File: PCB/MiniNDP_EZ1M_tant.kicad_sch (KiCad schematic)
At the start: 16 parts, among them J1 Conn_02x20_Odd_Even, U1 AS6C8008_TSOPII, U2 HC238, U3 4040, U4 FCT841

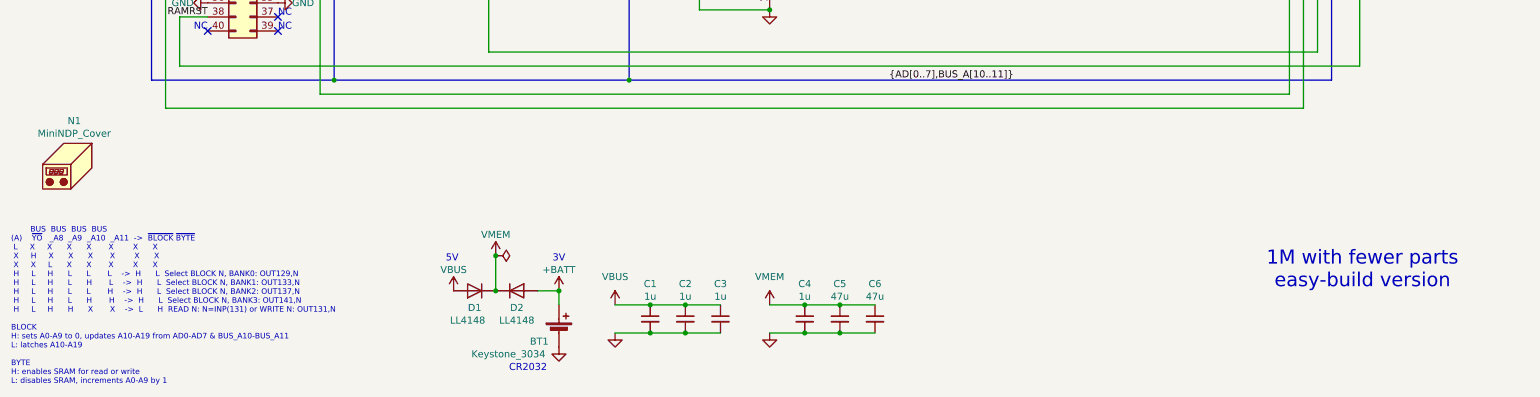
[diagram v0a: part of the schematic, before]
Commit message: make EZ1M the default
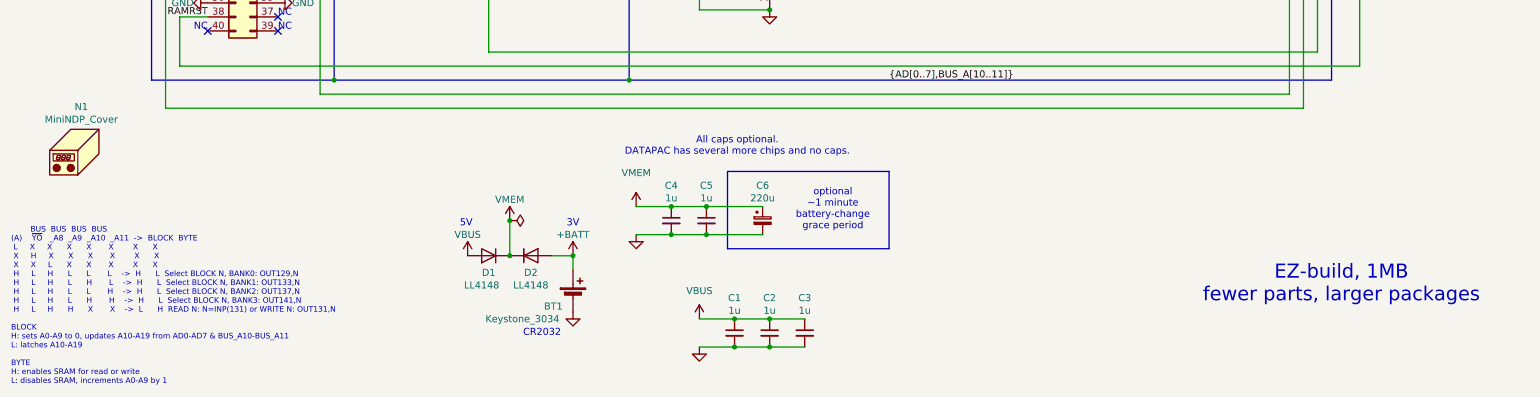
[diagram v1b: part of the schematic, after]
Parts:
- removed C6: 47u, 000_LOCAL:C_1206, symbol 000_LOCAL:C
- added C4: 1u, 000_LOCAL:C_0805, symbol 000_LOCAL:C
- C6: renamed from C5; value 47u -> 220u; footprint 000_LOCAL:C_1206 -> 000_LOCAL:CP_6032; symbol 000_LOCAL:C -> 000_LOCAL:C_Polarized; MPN C3216X5R1E476M160DC -> TAJC227K010RNJ
- renumbered C4 to C5
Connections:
- net GND: now also C4.2
- net VMEM: now also C4.1
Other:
- note added: "All caps optional. DATAPAC has several more chips and no caps."
- note added: "BUS BUS BUS BUS (A) ~{YO} _A8 _A9 _A10 _A11 -> BLOCK BYTE L X X X X X X X X H X X X X X X X X L X X X X X H L H L L L -> H L Select BLOCK N, BANK0: OUT129,N H L H L H L -> H L Select BLOCK N, BANK1: OUT133,N H L H L L H -> H L Select BLOCK N, BANK2: OUT137,N H L H L H H -> H L Select BLOCK N, BANK3: OUT141,N H L H H X X -> L H READ N: N=INP(131) or WRITE N: OUT131,N BLOCK H: sets A0-A9 to 0, upda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"
- note added: "EZ-build, 1MB fewer parts, larger packages"
- note added: "optional ~1 minute battery-change grace period"
- note removed: "1M with fewer parts easy-build version"
- note removed: "BUS BUS BUS BUS (A) ~{YO} _A8 _A9 _A10 _A11 -> ~{BLOCK} ~{BYTE} L X X X X X X X X H X X X X X X X X L X X X X X H L H L L L -> H L Select BLOCK N, BANK0: OUT129,N H L H L H L -> H L Select BLOCK N, BANK1: OUT133,N H L H L L H -> H L Select BLOCK N, BANK2: OUT137,N H L H L H H -> H L Select BLOCK N, BANK3: OUT141,N H L H H X X -> L H READ N: N=INP(131) or WRITE N: OUT131,N BLOCK H: sets A0-A9 to 0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"
- title: MiniNDP EZ1M -> MiniNDP
- moved on the sheet: BT1, C1, C2, C3, C5, D1, D2, N1

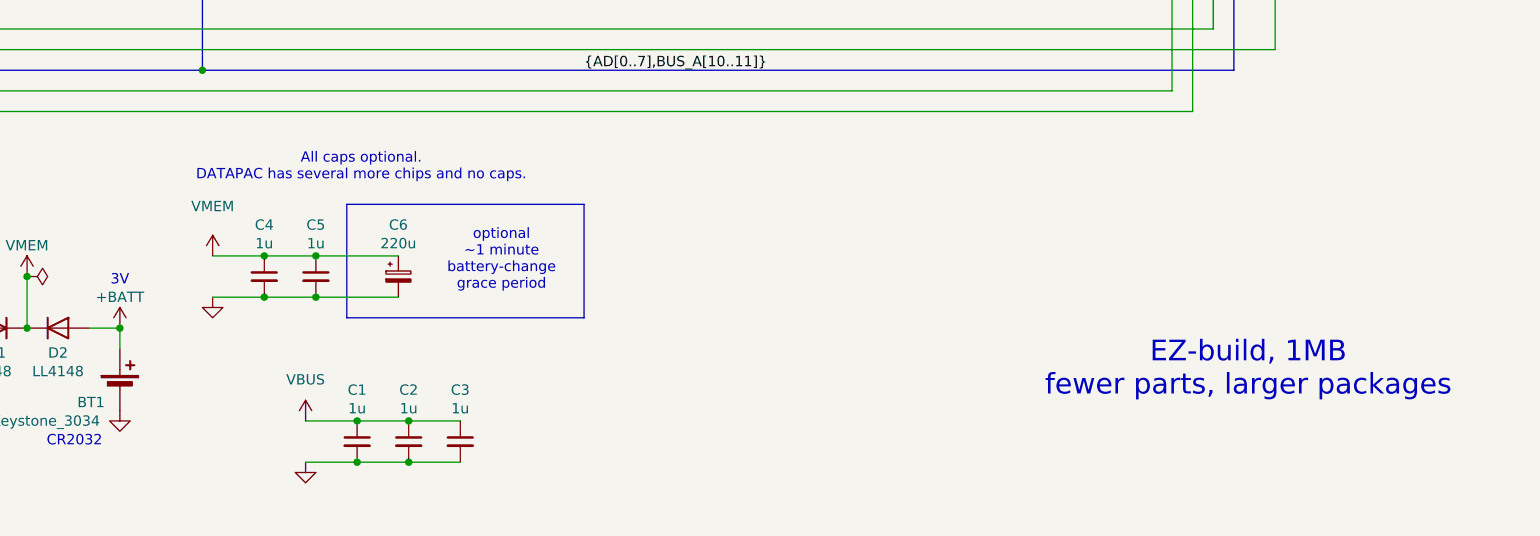
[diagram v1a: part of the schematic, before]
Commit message: re-add inrush resistor to EZ1M_tant
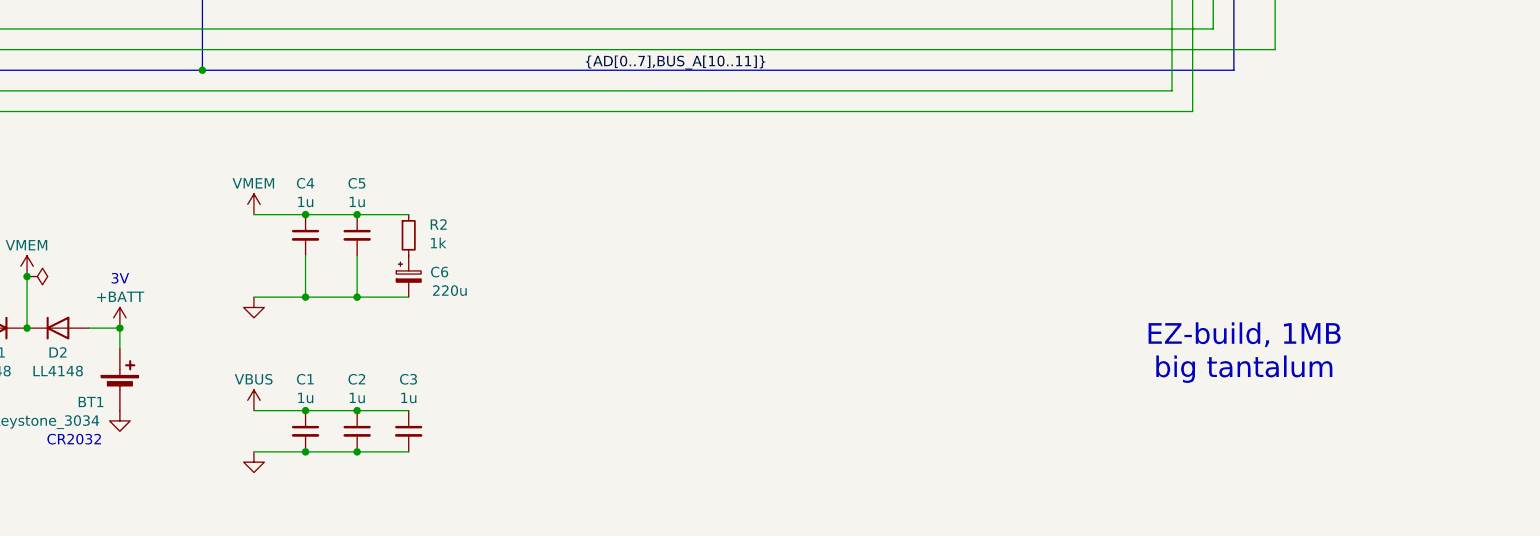
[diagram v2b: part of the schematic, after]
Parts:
- added R2: 1k, 000_LOCAL:R_0805, symbol 000_LOCAL:R
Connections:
- net VMEM: now also R2.1; no longer C6.1
- new net: C6.1, R2.2
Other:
- note added: "EZ-build, 1MB big tantalum"
- note removed: "All caps optional. DATAPAC has several more chips and no caps."
- note removed: "EZ-build, 1MB fewer parts, larger packages"
- note removed: "optional ~1 minute battery-change grace period"
- moved on the sheet: C1, C2, C3, C4, C5, C6
